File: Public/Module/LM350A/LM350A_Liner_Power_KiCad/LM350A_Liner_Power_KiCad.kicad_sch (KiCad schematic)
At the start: 4 parts, among them U1 LM350_TO220

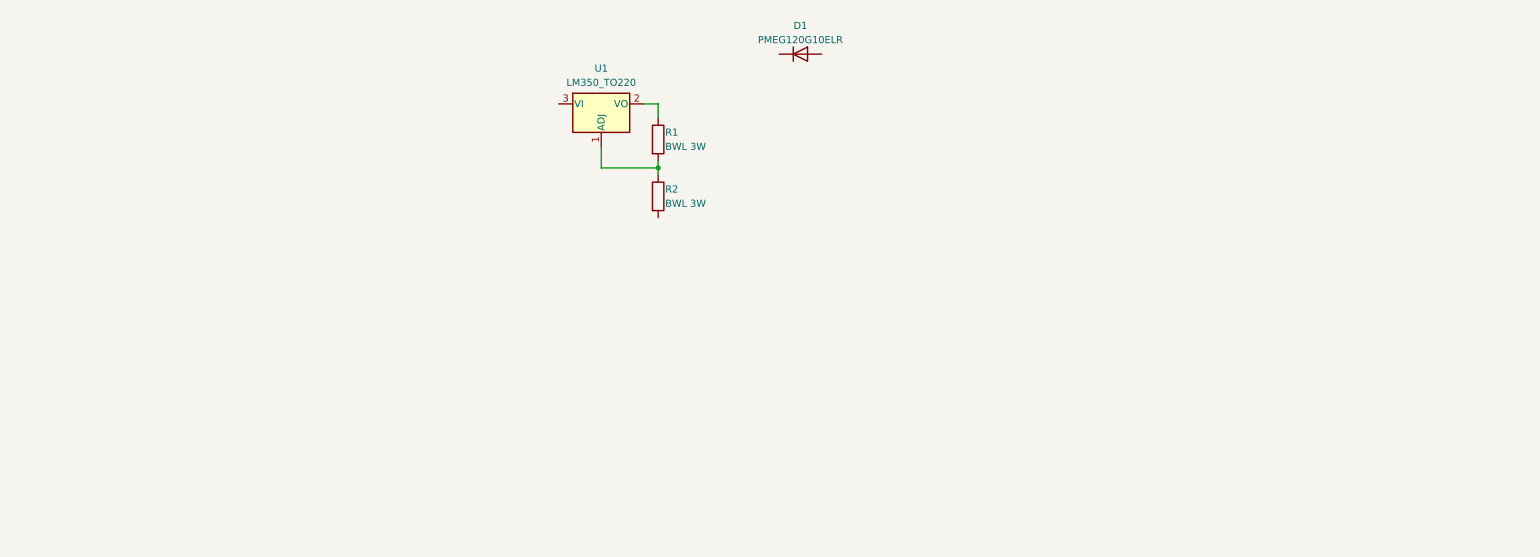
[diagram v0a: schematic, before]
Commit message: Update LM350 Module
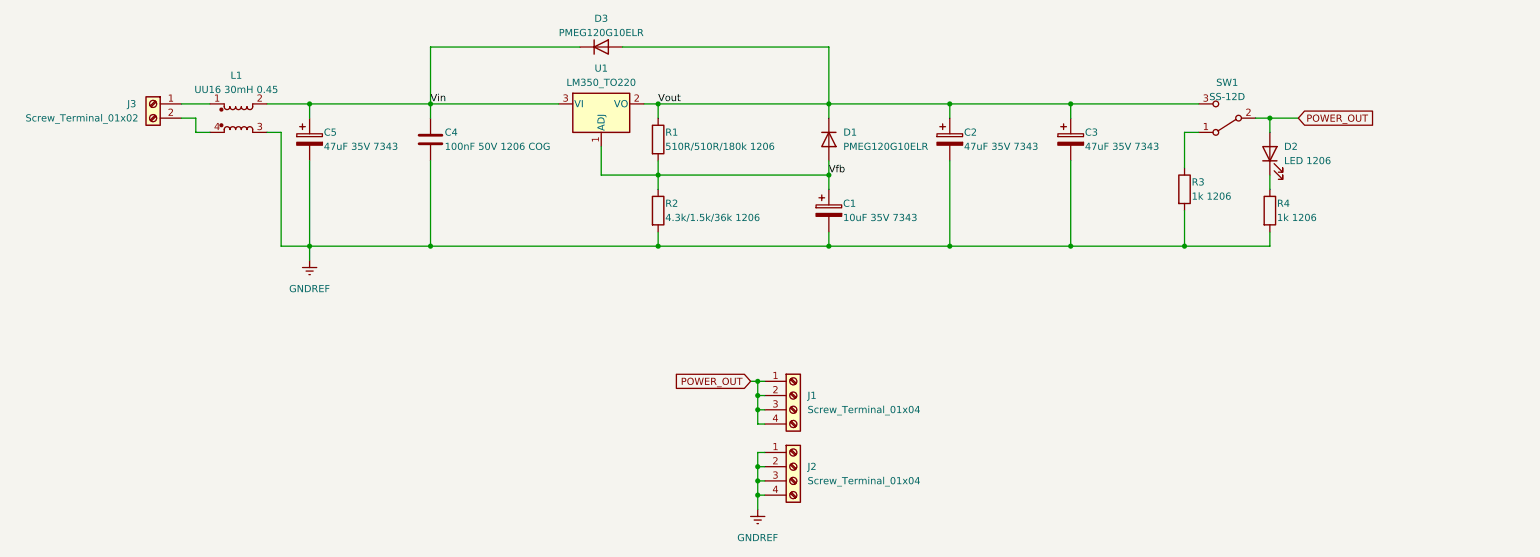
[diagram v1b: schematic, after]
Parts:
- added C1: 10uF 35V 7343, Capacitor_Tantalum_SMD:CP_EIA-7343-31_Kemet-D, symbol Device:C_Polarized
- added C2, C3, C5: 47uF 35V 7343, Capacitor_Tantalum_SMD:CP_EIA-7343-31_Kemet-D, symbol Device:C_Polarized
- added C4: 100nF 50V 1206 COG, Capacitor_SMD:C_1206_3216Metric, symbol Device:C
- added D2: LED 1206, LED_SMD:LED_1206_3216Metric, symbol Device:LED
- added D3: PMEG120G10ELR, Diode_SMD:D_SOD-123, symbol Device:D
- added J1, J2: Screw_Terminal_01x04, Customer_Connector:2EDG-5.08mm_4P_Horizontal, symbol Connector:Screw_Terminal_01x04
- added J3: Screw_Terminal_01x02, Customer_Connector:2EDG-5.08mm_2P_Horizontal, symbol Connector:Screw_Terminal_01x02
- added L1: UU16 30mH 0.45, Customer_Passive:Inductor_Coupled_THT_UF16, symbol Device:L_Coupled_1243
- added R3, R4: 1k 1206, Resistor_SMD:R_1206_3216Metric, symbol Device:R
- added SW1: SS-12D, Customer_Switch:SS-12D, symbol Switch:SW_SPDT
- D1: footprint (none) -> Diode_SMD:D_SOD-123
- R1: value BWL 3W -> 510R/510R/180k 1206; footprint (none) -> Resistor_SMD:R_1206_3216Metric
- R2: value BWL 3W -> 4.3k/1.5k/36k 1206; footprint (none) -> Resistor_SMD:R_1206_3216Metric
- U1: footprint Package_TO_SOT_THT:TO-220-3_Vertical -> Package_TO_SOT_THT:TO-220-3_Horizontal_TabUp
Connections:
- net Vfb: now reaches R1.2, R2.1, U1.1 (ADJ)
- net Vfb: now also D1.2 (A), C1.1
- net Vout: now reaches R1.1, U1.2 (VO)
- net Vout: now also D1.1 (K), C2.1, C3.1, D3.2 (A), SW1.3 (C)
- net Vin: now reaches U1.3 (VI)
- net Vin: now also C4.1, C5.1, D3.1 (K), L1.2
- net GNDREF: now reaches R2.2
- net GNDREF: now also C1.2, C2.2, C3.2, C4.2, C5.2, J2.1 (Pin_1), J2.2 (Pin_2), J2.3 (Pin_3), J2.4 (Pin_4), L1.3, R3.2, R4.2
- new net: D2.1 (K), R4.1
- new net: J3.1 (Pin_1), L1.1
- new net: J3.2 (Pin_2), L1.4
- new net: R3.1, SW1.1 (A)
- new net POWER_OUT: D2.2 (A), J1.1 (Pin_1), J1.2 (Pin_2), J1.3 (Pin_3), J1.4 (Pin_4), SW1.2 (B)
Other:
- moved on the sheet: D1, R2

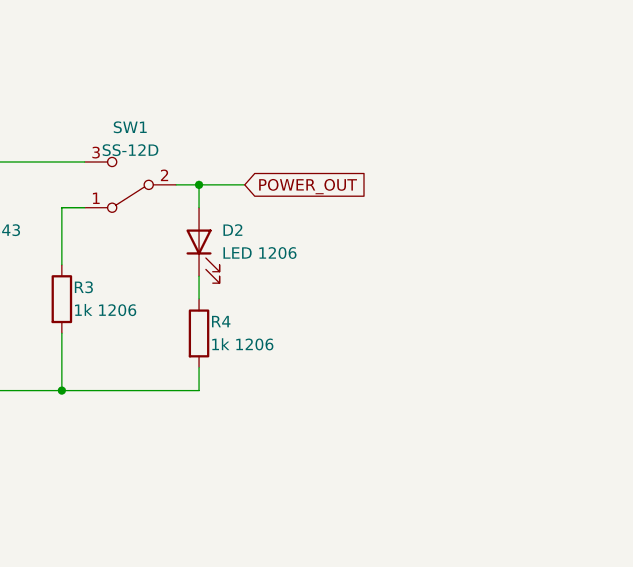
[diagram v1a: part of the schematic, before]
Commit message: Update LM350A Moudle
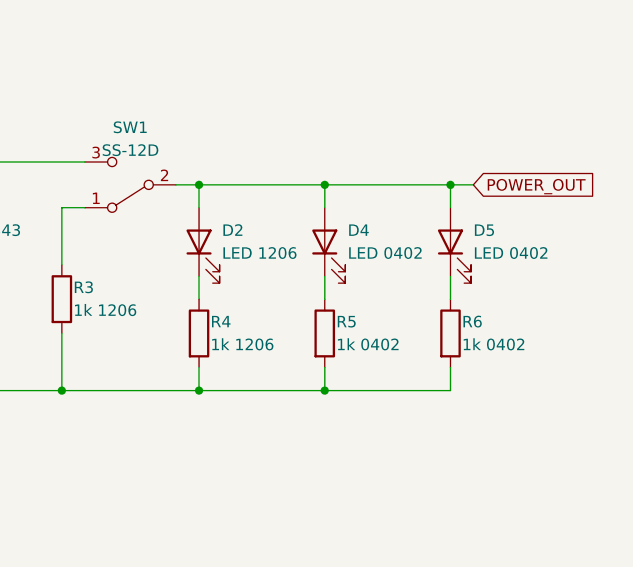
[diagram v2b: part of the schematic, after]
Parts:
- added D4, D5: LED 0402, Customer_Passive:LED_0402_Bottom, symbol Device:LED
- added R5, R6: 1k 0402, Resistor_SMD:R_0402_1005Metric, symbol Device:R
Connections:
- net GNDREF: now also R5.2, R6.2
- net POWER_OUT: now also D4.2 (A), D5.2 (A)
- new net: D4.1 (K), R5.1
- new net: D5.1 (K), R6.1
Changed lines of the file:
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@@
   (junction (at 160.02 104.14) (diameter 0) (color 0 0 0 0)
   )
+  (junction (at 266.7 81.28) (diameter 0) (color 0 0 0 0)
+  )
   (junction (at 147.32 146.05) (diameter 0) (color 0 0 0 0)
   )
   (junction (at 88.9 78.74) (diameter 0) (color 0 0 0 0)
   )
+  (junction (at 252.73 81.28) (diameter 0) (color 0 0 0 0)
+  )
   (junction (at 160.02 78.74) (diameter 0) (color 0 0 0 0)
   )
+  (junction (at 252.73 104.14) (diameter 0) (color 0 0 0 0)
+  )
   (junction (at 203.2 104.14) (diameter 0) (color 0 0 0 0)
   )
@@
   (junction (at 67.31 78.74) (diameter 0) (color 0 0 0 0)
   )
+  (junction (at 238.76 104.14) (diameter 0) (color 0 0 0 0)
+  )
   (junction (at 238.76 81.28) (diameter 0) (color 0 0 0 0)
   )
@@
   (junction (at 147.32 128.27) (diameter 0) (color 0 0 0 0)
   )
+  (wire (pts (xy 252.73 81.28) (xy 252.73 83.82))
+    (stroke (width 0) (type default))
+  )
   (wire (pts (xy 147.32 128.27) (xy 148.59 128.27))
     (stroke (width 0) (type default))
@@
     (stroke (width 0) (type default))
   )
+  (wire (pts (xy 266.7 81.28) (xy 266.7 83.82))
+    (stroke (width 0) (type default))
+  )
+  (wire (pts (xy 266.7 101.6) (xy 266.7 104.14))
+    (stroke (width 0) (type default))
+  )
   (wire (pts (xy 46.99 83.82) (xy 49.53 83.82))
     (stroke (width 0) (type default))
@@
     (stroke (width 0) (type default))
   )
+  (wire (pts (xy 252.73 81.28) (xy 266.7 81.28))
+    (stroke (width 0) (type default))
+  )
+  (wire (pts (xy 238.76 104.14) (xy 252.73 104.14))
+    (stroke (width 0) (type default))
+  )
   (wire (pts (xy 67.31 81.28) (xy 67.31 78.74))
     (stroke (width 0) (type default))
@@
     (stroke (width 0) (type default))
   )
+  (wire (pts (xy 252.73 91.44) (xy 252.73 93.98))
+    (stroke (width 0) (type default))
+  )
   (wire (pts (xy 129.54 101.6) (xy 129.54 104.14))
     (stroke (width 0) (type default))
@@
     (stroke (width 0) (type default))
   )
-  (wire (pts (xy 238.76 81.28) (xy 243.84 81.28))
+  (wire (pts (xy 238.76 81.28) (xy 252.73 81.28))
     (stroke (width 0) (type default))
   )
@@
     (stroke (width 0) (type default))
   )
+  (wire (pts (xy 266.7 81.28) (xy 269.24 81.28))
+    (stroke (width 0) (type default))
+  )
   (wire (pts (xy 223.52 97.79) (xy 223.52 104.14))
     (stroke (width 0) (type default))
@@
     (stroke (width 0) (type default))
   )
+  (wire (pts (xy 252.73 104.14) (xy 266.7 104.14))
+    (stroke (width 0) (type default))
+  )
   (wire (pts (xy 67.31 88.9) (xy 67.31 104.14))
     (stroke (width 0) (type default))
@@
     (stroke (width 0) (type default))
   )
+  (wire (pts (xy 266.7 91.44) (xy 266.7 93.98))
+    (stroke (width 0) (type default))
+  )
   (wire (pts (xy 238.76 101.6) (xy 238.76 104.14))
     (stroke (width 0) (type default))
   )
   (wire (pts (xy 123.19 68.58) (xy 160.02 68.58))
+    (stroke (width 0) (type default))
+  )
+  (wire (pts (xy 252.73 101.6) (xy 252.73 104.14))
     (stroke (width 0) (type default))
   )
@@
     )
   )
-  (global_label "POWER_OUT" (shape input) (at 243.84 81.28 0) (fields_autoplaced)
+  (global_label "POWER_OUT" (shape input) (at 269.24 81.28 0) (fields_autoplaced)
     (effects (font (size 1.27 1.27)) (justify left))
-    (property "Intersheetrefs" "${INTERSHEET_REFS}" (at 257.8923 81.28 0)
+    (property "Intersheetrefs" "${INTERSHEET_REFS}" (at 283.2923 81.28 0)
       (effects (font (size 1.27 1.27)) (justify left) hide)
     )
@@
         (path "/0387899e-e136-4bc9-844e-8783e3da867c"
           (reference "D3") (unit 1)
+        )
+      )
+    )
+  )
+  (symbol (lib_id "Device:R") (at 252.73 97.79 0) (unit 1)
+    (in_bom yes) (on_board yes) (dnp no)
+    (property "Reference" "R5" (at 254 96.52 0)
+      (effects (font (size 1.27 1.27)) (justify left))
+    )
+    (property "Value" "1k 0402" (at 254 99.06 0)
+      (effects (font (size 1.27 1.27)) (justify left))
+    )
+    (property "Footprint" "Resistor_SMD:R_0402_1005Metric" (at 250.952 97.79 90)
+      (effects (font (size 1.27 1.27)) hide)
+    )
+    (property "Datasheet" "~" (at 252.73 97.79 0)
+      (effects (font (size 1.27 1.27)) hide)
+    )
+    (pin "1")
+    (pin "2")
+    (instances
+      (project "LM350A_Liner_Power_KiCad"
+        (path "/0387899e-e136-4bc9-844e-8783e3da867c"
+          (reference "R5") (unit 1)
         )
       )
@@
     )
   )
+  (symbol (lib_id "Device:LED") (at 252.73 87.63 90) (unit 1)
+    (in_bom yes) (on_board yes) (dnp no)
+    (property "Reference" "D4" (at 255.27 86.36 90)
+      (effects (font (size 1.27 1.27)) (justify right))
+    )
+    (property "Value" "LED 0402" (at 255.27 88.9 90)
+      (effects (font (size 1.27 1.27)) (justify right))
+    )
+    (property "Footprint" "Customer_Passive:LED_0402_Bottom" (at 252.73 87.63 0)
+      (effects (font (size 1.27 1.27)) hide)
+    )
+    (property "Datasheet" "~" (at 252.73 87.63 0)
+      (effects (font (size 1.27 1.27)) hide)
+    )
+    (pin "1")
+    (pin "2")
+    (instances
+      (project "LM350A_Liner_Power_KiCad"
+        (path "/0387899e-e136-4bc9-844e-8783e3da867c"
+          (reference "D4") (unit 1)
+        )
+      )
+    )
+  )
   (symbol (lib_id "Switch:SW_SPDT") (at 231.14 81.28 180) (unit 1)
     (in_bom yes) (on_board yes) (dnp no)
@@
         (path "/0387899e-e136-4bc9-844e-8783e3da867c"
           (reference "SW1") (unit 1)
+        )
+      )
+    )
+  )
+  (symbol (lib_id "Device:LED") (at 266.7 87.63 90) (unit 1)
+    (in_bom yes) (on_board yes) (dnp no)
+    (property "Reference" "D5" (at 269.24 86.36 90)
+      (effects (font (size 1.27 1.27)) (justify right))
+    )
+    (property "Value" "LED 0402" (at 269.24 88.9 90)
+      (effects (font (size 1.27 1.27)) (justify right))
+    )
+    (property "Footprint" "Customer_Passive:LED_0402_Bottom" (at 266.7 87.63 0)
+      (effects (font (size 1.27 1.27)) hide)
+    )
+    (property "Datasheet" "~" (at 266.7 87.63 0)
+      (effects (font (size 1.27 1.27)) hide)
+    )
+    (pin "1")
+    (pin "2")
+    (instances
+      (project "LM350A_Liner_Power_KiCad"
+        (path "/0387899e-e136-4bc9-844e-8783e3da867c"
+          (reference "D5") (unit 1)
         )
       )
@@
         )
       )
+    )
+  )
+  (symbol (lib_id "Device:R") (at 266.7 97.79 0) (unit 1)
+    (in_bom yes) (on_board yes) (dnp no)
+    (property "Reference" "R6" (at 267.97 96.52 0)
+      (effects (font (size 1.27 1.27)) (justify left))
+    )
+    (property "Value" "1k 0402" (at 267.97 99.06 0)
+      (effects (font (size 1.27 1.27)) (justify left))
+    )
+    (property "Footprint" "Resistor_SMD:R_0402_1005Metric" (at 264.922 97.79 90)
+      (effects (font (size 1.27 1.27)) hide)
+    )
+    (property "Datasheet" "~" (at 266.7 97.79 0)
+      (effects (font (size 1.27 1.27)) hide)
+    )
+    (pin "1")
+    (pin "2")
+    (instances
+      (project "LM350A_Liner_Power_KiCad"
+        (path "/0387899e-e136-4bc9-844e-8783e3da867c"
+          (reference "R6") (unit 1)
+        )
+      )

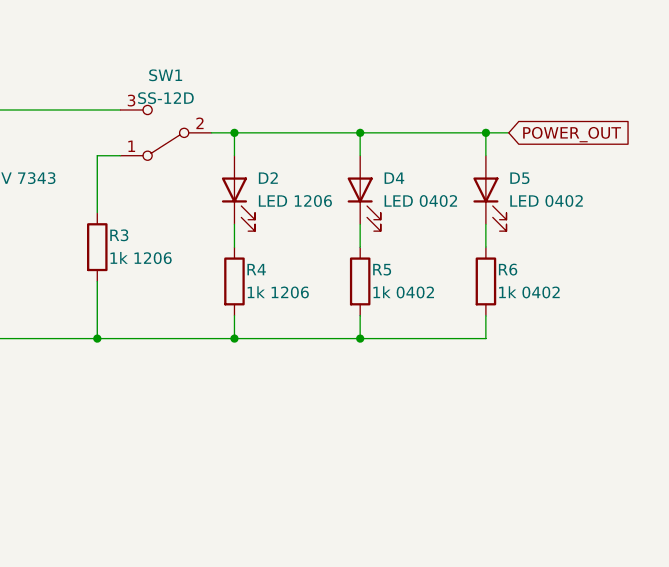
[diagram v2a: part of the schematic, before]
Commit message: Update LM350 Module
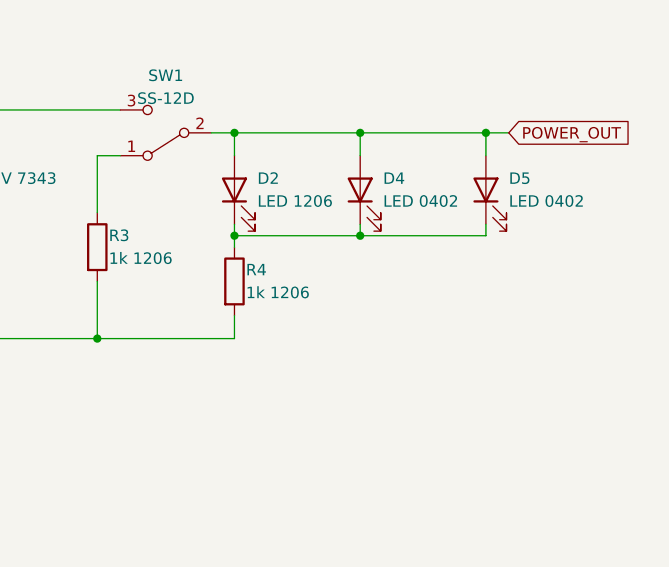
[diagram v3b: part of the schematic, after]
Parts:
- removed R5, R6: 1k 0402, Resistor_SMD:R_0402_1005Metric, symbol Device:R
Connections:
- net at D2.1 (K), R4.1: now also D4.1 (K), D5.1 (K)
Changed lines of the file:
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@@
   (junction (at 266.7 81.28) (diameter 0) (color 0 0 0 0)
   )
+  (junction (at 252.73 92.71) (diameter 0) (color 0 0 0 0)
+  )
   (junction (at 147.32 146.05) (diameter 0) (color 0 0 0 0)
   )
@@
   (junction (at 160.02 78.74) (diameter 0) (color 0 0 0 0)
   )
-  (junction (at 252.73 104.14) (diameter 0) (color 0 0 0 0)
-  )
   (junction (at 203.2 104.14) (diameter 0) (color 0 0 0 0)
   )
@@
   (junction (at 67.31 78.74) (diameter 0) (color 0 0 0 0)
   )
-  (junction (at 238.76 104.14) (diameter 0) (color 0 0 0 0)
+  (junction (at 238.76 92.71) (diameter 0) (color 0 0 0 0)
   )
   (junction (at 238.76 81.28) (diameter 0) (color 0 0 0 0)
@@
     (stroke (width 0) (type default))
   )
+  (wire (pts (xy 266.7 92.71) (xy 252.73 92.71))
+    (stroke (width 0) (type default))
+  )
   (wire (pts (xy 147.32 128.27) (xy 148.59 128.27))
     (stroke (width 0) (type default))
@@
     (stroke (width 0) (type default))
   )
-  (wire (pts (xy 266.7 101.6) (xy 266.7 104.14))
-    (stroke (width 0) (type default))
-  )
   (wire (pts (xy 46.99 83.82) (xy 49.53 83.82))
     (stroke (width 0) (type default))
@@
     (stroke (width 0) (type default))
   )
+  (wire (pts (xy 252.73 91.44) (xy 252.73 92.71))
+    (stroke (width 0) (type default))
+  )
   (wire (pts (xy 148.59 148.59) (xy 147.32 148.59))
     (stroke (width 0) (type default))
@@
     (stroke (width 0) (type default))
   )
-  (wire (pts (xy 238.76 104.14) (xy 252.73 104.14))
-    (stroke (width 0) (type default))
-  )
   (wire (pts (xy 67.31 81.28) (xy 67.31 78.74))
     (stroke (width 0) (type default))
@@
     (stroke (width 0) (type default))
   )
-  (wire (pts (xy 238.76 91.44) (xy 238.76 93.98))
+  (wire (pts (xy 238.76 91.44) (xy 238.76 92.71))
     (stroke (width 0) (type default))
   )
@@
     (stroke (width 0) (type default))
   )
-  (wire (pts (xy 252.73 91.44) (xy 252.73 93.98))
-    (stroke (width 0) (type default))
-  )
   (wire (pts (xy 129.54 101.6) (xy 129.54 104.14))
     (stroke (width 0) (type default))
@@
     (stroke (width 0) (type default))
   )
+  (wire (pts (xy 266.7 91.44) (xy 266.7 92.71))
+    (stroke (width 0) (type default))
+  )
   (wire (pts (xy 181.61 78.74) (xy 160.02 78.74))
     (stroke (width 0) (type default))
@@
     (stroke (width 0) (type default))
   )
+  (wire (pts (xy 252.73 92.71) (xy 238.76 92.71))
+    (stroke (width 0) (type default))
+  )
   (wire (pts (xy 148.59 140.97) (xy 147.32 140.97))
     (stroke (width 0) (type default))
@@
     (stroke (width 0) (type default))
   )
-  (wire (pts (xy 252.73 104.14) (xy 266.7 104.14))
+  (wire (pts (xy 238.76 92.71) (xy 238.76 93.98))
     (stroke (width 0) (type default))
   )
@@
     (stroke (width 0) (type default))
   )
-  (wire (pts (xy 266.7 91.44) (xy 266.7 93.98))
-    (stroke (width 0) (type default))
-  )
   (wire (pts (xy 238.76 101.6) (xy 238.76 104.14))
     (stroke (width 0) (type default))
   )
   (wire (pts (xy 123.19 68.58) (xy 160.02 68.58))
-    (stroke (width 0) (type default))
-  )
-  (wire (pts (xy 252.73 101.6) (xy 252.73 104.14))
     (stroke (width 0) (type default))
   )
@@
     )
   )
-  (symbol (lib_id "Device:R") (at 252.73 97.79 0) (unit 1)
-    (in_bom yes) (on_board yes) (dnp no)
-    (property "Reference" "R5" (at 254 96.52 0)
-      (effects (font (size 1.27 1.27)) (justify left))
-    )
-    (property "Value" "1k 0402" (at 254 99.06 0)
-      (effects (font (size 1.27 1.27)) (justify left))
-    )
-    (property "Footprint" "Resistor_SMD:R_0402_1005Metric" (at 250.952 97.79 90)
-      (effects (font (size 1.27 1.27)) hide)
-    )
-    (property "Datasheet" "~" (at 252.73 97.79 0)
-      (effects (font (size 1.27 1.27)) hide)
-    )
-    (pin "1")
-    (pin "2")
-    (instances
-      (project "LM350A_Liner_Power_KiCad"
-        (path "/0387899e-e136-4bc9-844e-8783e3da867c"
-          (reference "R5") (unit 1)
-        )
-      )
-    )
-  )
   (symbol (lib_id "Device:L_Coupled_1243") (at 54.61 81.28 0) (unit 1)
     (in_bom yes) (on_board yes) (dnp no) (fields_autoplaced)
@@
         )
       )
-    )
-  )
-  (symbol (lib_id "Device:R") (at 266.7 97.79 0) (unit 1)
-    (in_bom yes) (on_board yes) (dnp no)
-    (property "Reference" "R6" (at 267.97 96.52 0)
-      (effects (font (size 1.27 1.27)) (justify left))
-    )
-    (property "Value" "1k 0402" (at 267.97 99.06 0)
-      (effects (font (size 1.27 1.27)) (justify left))
-    )
-    (property "Footprint" "Resistor_SMD:R_0402_1005Metric" (at 264.922 97.79 90)
-      (effects (font (size 1.27 1.27)) hide)
-    )
-    (property "Datasheet" "~" (at 266.7 97.79 0)
-      (effects (font (size 1.27 1.27)) hide)
-    )
-    (pin "1")
-    (pin "2")
-    (instances
-      (project "LM350A_Liner_Power_KiCad"
-        (path "/0387899e-e136-4bc9-844e-8783e3da867c"
-          (reference "R6") (unit 1)
-        )
-      )
